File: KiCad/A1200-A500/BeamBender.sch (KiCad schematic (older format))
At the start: 25 parts, among them J1 4-1734742-0, J2 HDMI_A_1.4, J3 STX-3501-3N, U1 LM1117-3.3, U3 ADV7513BSWZ

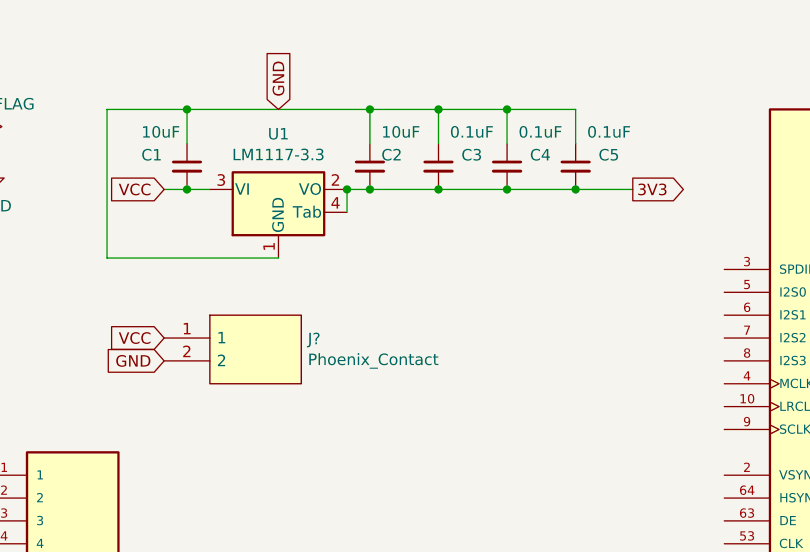
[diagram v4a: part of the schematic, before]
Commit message: Added Polarized electrolytical capacitors for 3V3-power
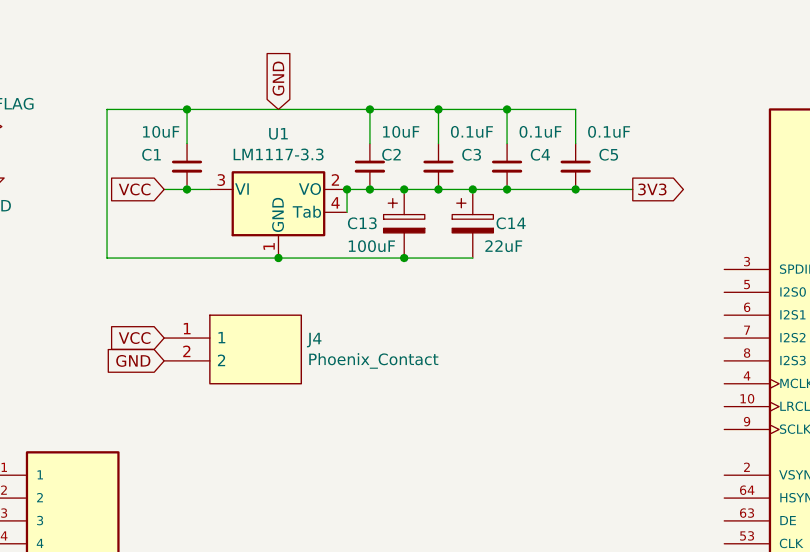
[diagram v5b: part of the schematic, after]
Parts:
- added C13: 100uF, Capacitor_SMD:CP_Elec_6.3x7.7, symbol Device:CP
- added C14: 22uF, Capacitor_SMD:CP_Elec_5x5.8, symbol Device:CP
- gave numbers to parts that had none: 1
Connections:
- net 3V3: now also C13.1, C14.1
- net GND: now also C13.2, C14.2
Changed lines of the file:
@@
 $EndComp
 Wire Wire Line
-	3150 1150 3450 1150
+	3150 1150 3300 1150
 Connection ~ 3450 1150
 Wire Wire Line
@@
 $EndComp
 Wire Wire Line
-	2850 1150 3150 1150
+	2850 1150 3000 1150
 Connection ~ 3150 800
 Wire Wire Line
@@
 	10300 1100 10650 1100
 $Comp
-L BeamBender:Phoenix_Contact J?
+L BeamBender:Phoenix_Contact J4
 U 1 1 654E9506
 P 2350 1850
-F 0 "J?" H 2578 1896 50  0000 L CNN
+F 0 "J4" H 2578 1896 50  0000 L CNN
 F 1 "Phoenix_Contact" H 2578 1805 50  0000 L CNN
 F 2 "BeamBender:Phoenix_Contact" H 2600 2000 50  0001 L CNN
@@
 Text GLabel 1950 1900 0    50   Input ~ 0
 GND
+$Comp
+L Device:CP C13
+U 1 1 65230529
+P 3000 1300
+F 0 "C13" H 2750 1300 50  0000 L CNN
+F 1 "100uF" H 2750 1200 50  0000 L CNN
+F 2 "Capacitor_SMD:CP_Elec_6.3x7.7" H 3038 1150 50  0001 C CNN
+F 3 "~" H 3000 1300 50  0001 C CNN
+	1    3000 1300
+	1    0    0    -1
+$EndComp
+Connection ~ 3000 1150
+Wire Wire Line
+	3000 1150 3150 1150
+Wire Wire Line
+	2450 1450 3000 1450
+Connection ~ 2450 1450
+$Comp
+L Device:CP C14
+U 1 1 65238B23
+P 3300 1300
+F 0 "C14" H 3400 1300 50  0000 L CNN
+F 1 "22uF" H 3350 1200 50  0000 L CNN
+F 2 "Capacitor_SMD:CP_Elec_5x5.8" H 3338 1150 50  0001 C CNN
+F 3 "~" H 3300 1300 50  0001 C CNN
+	1    3300 1300
+	1    0    0    -1
+$EndComp
+Connection ~ 3300 1150
+Wire Wire Line
+	3300 1150 3450 1150
+Wire Wire Line
+	3000 1450 3300 1450
+Connection ~ 3000 1450
 $EndSCHEMATC

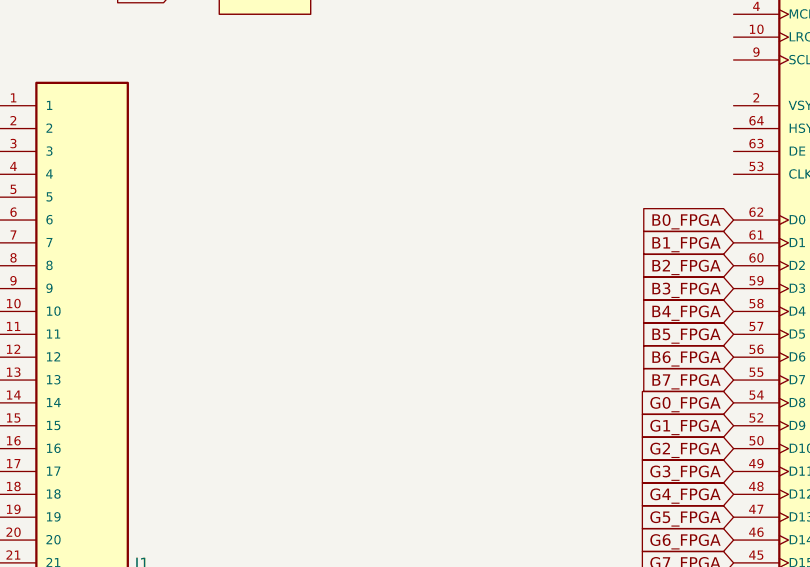
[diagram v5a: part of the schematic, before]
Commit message: Added Gowin FPGA GW1NR-UV9LQ144P
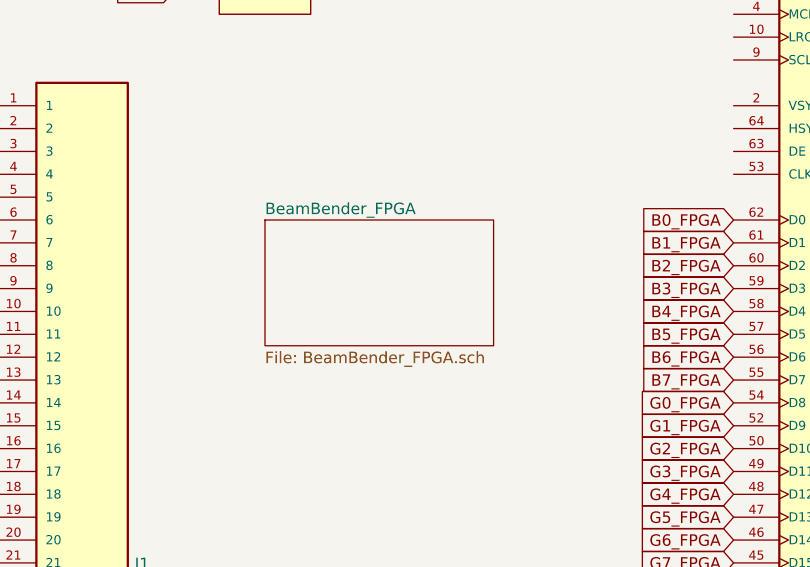
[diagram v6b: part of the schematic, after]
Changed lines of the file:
@@
 $Descr A4 11693 8268
 encoding utf-8
-Sheet 1 1
+Sheet 1 2
 Title ""
 Date ""
@@
 	3000 1450 3300 1450
 Connection ~ 3000 1450
+$Sheet
+S 2350 2900 1000 550
+U 6541C824
+F0 "BeamBender_FPGA" 50
+F1 "BeamBender_FPGA.sch" 50
+$EndSheet
 $EndSCHEMATC

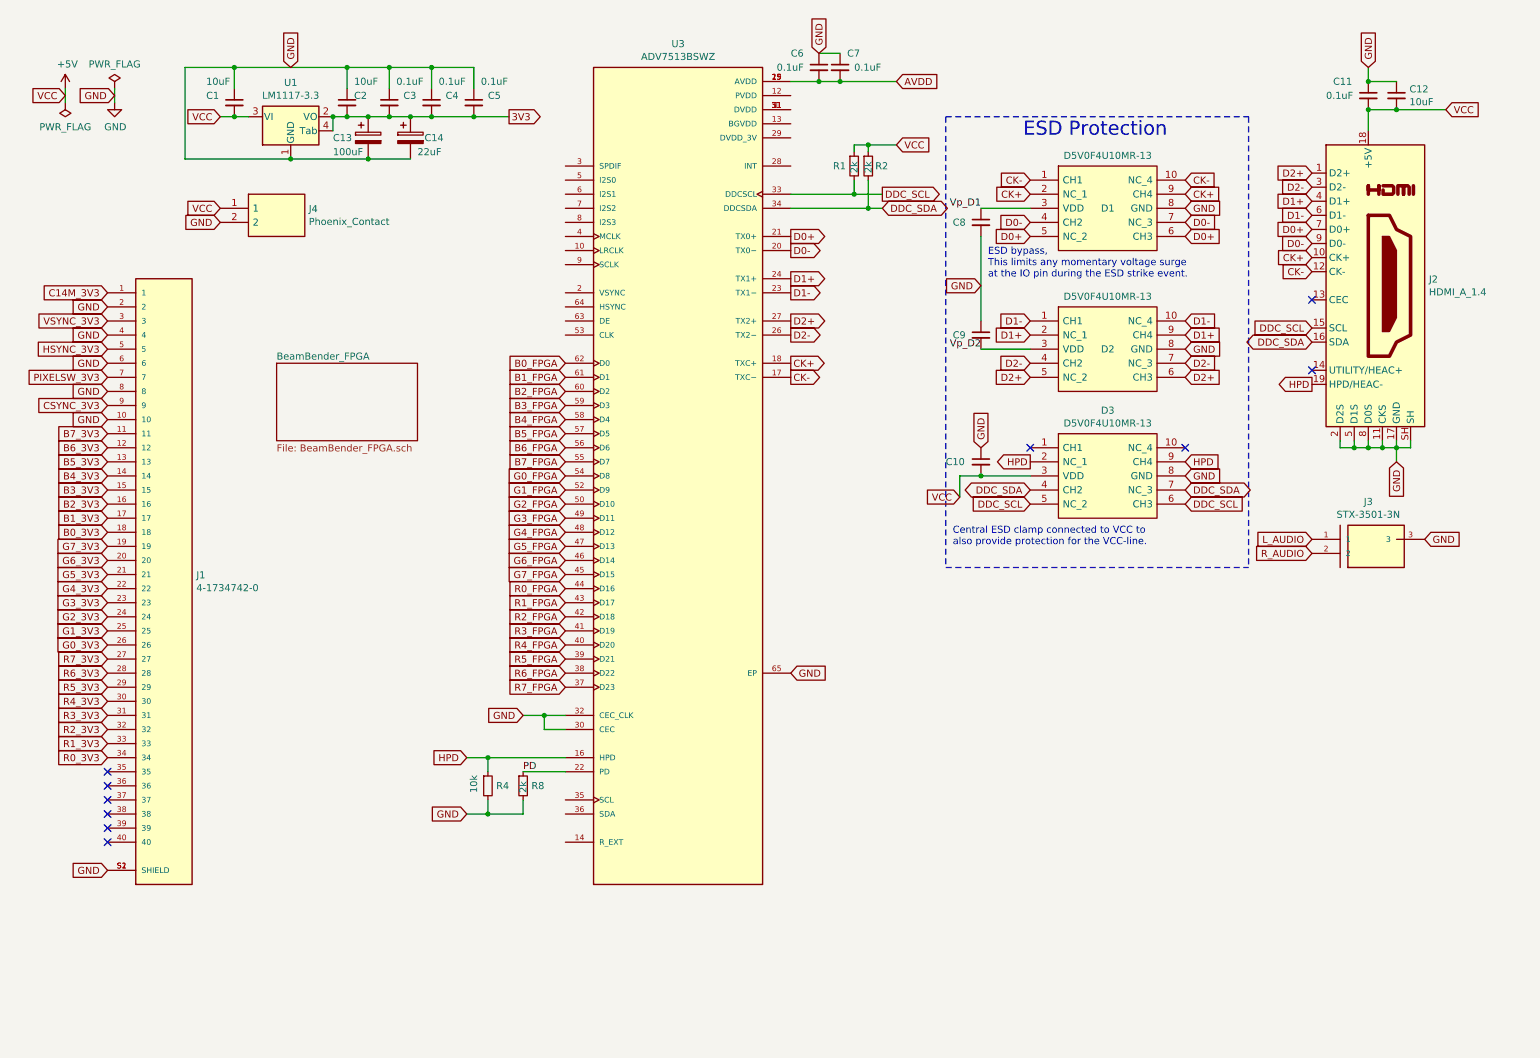
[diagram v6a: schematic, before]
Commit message: Added 27 MHz crystal oscillator X1 to GCLKT_4 pin and did some routing
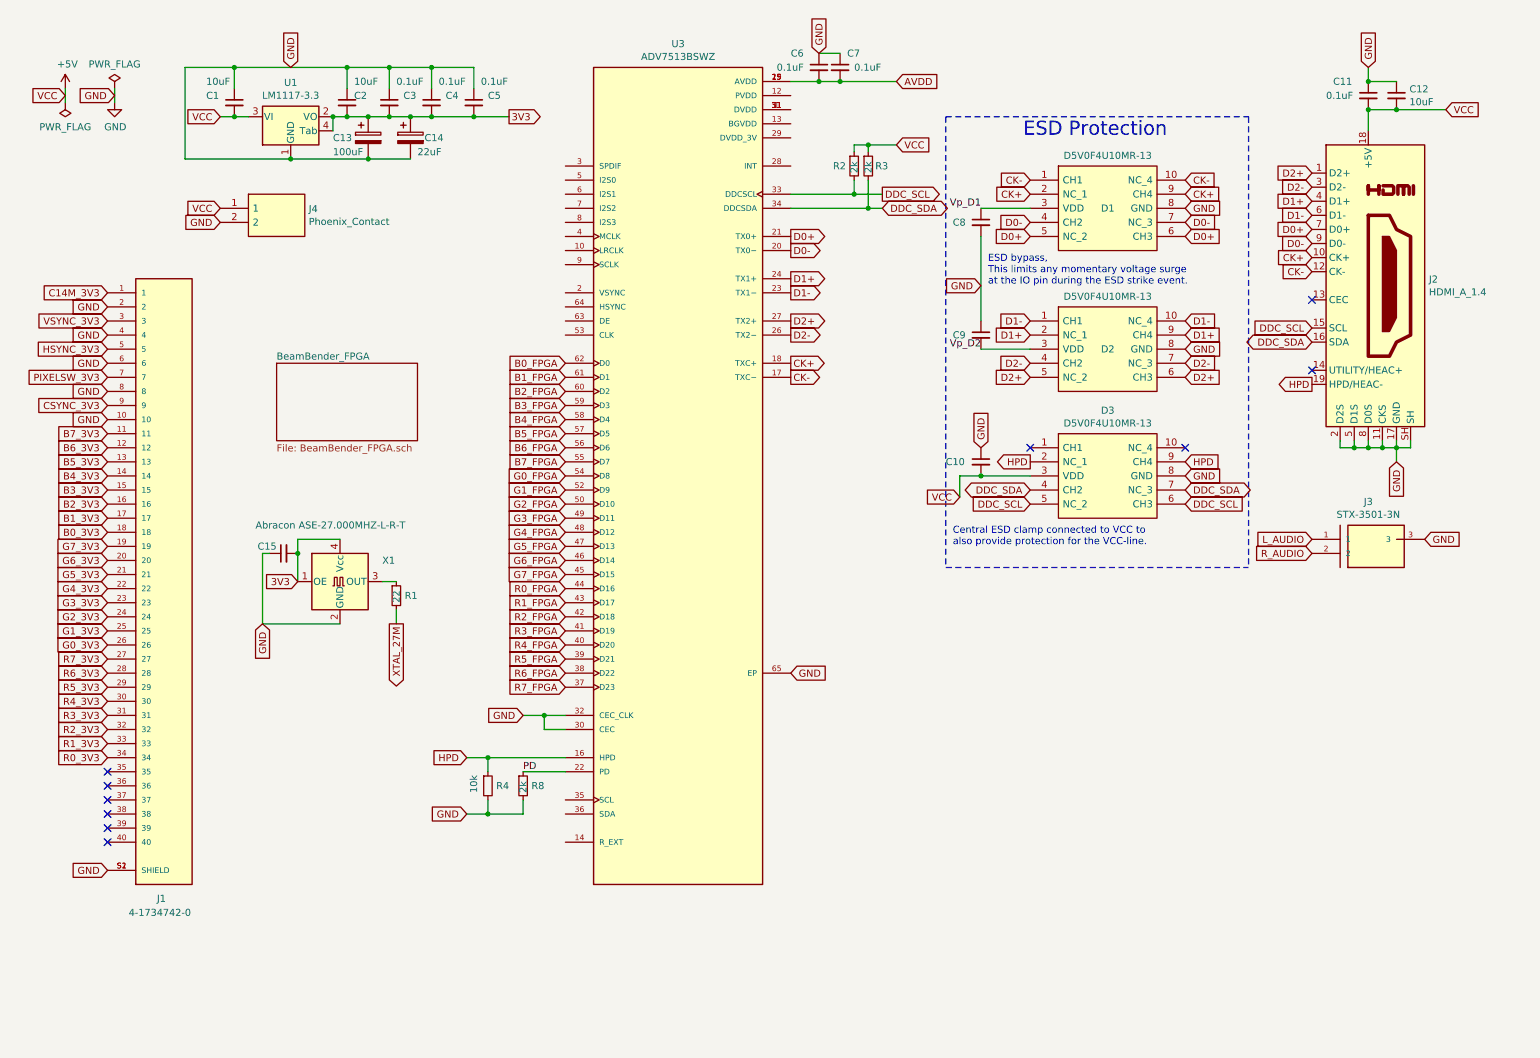
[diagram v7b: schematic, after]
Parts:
- added C15: 0.01uF, Capacitor_SMD:C_0603_1608Metric_Pad1.08x0.95mm_HandSolder, symbol Device:C_Small
- added R1: 22, Resistor_SMD:R_0603_1608Metric_Pad0.98x0.95mm_HandSolder, symbol Device:R_Small
- added X1: Abracon ASE-27.000MHZ-L-R-T, Oscillator:Oscillator_SMD_SeikoEpson_SG8002CE-4Pin_3.2x2.5mm, symbol Oscillator:SG-8002CE
- renumbered R1 to R2, R2 to R3
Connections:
- net 3V3: now also C15.2, X1.1 (OE), X1.4 (Vcc)
- net GND: now also C15.1, X1.2 (GND)
- new net: R1.1, X1.3 (OUT)
- new net XTAL_27M: R1.2
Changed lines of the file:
@@
 U 1 1 64F8C681
 P 1550 4400
-F 0 "J1" H 1780 4396 50  0000 L CNN
-F 1 "4-1734742-0" H 1780 4305 50  0000 L CNN
+F 0 "J1" H 1500 2100 50  0000 L CNN
+F 1 "4-1734742-0" H 1300 2000 50  0000 L CNN
 F 2 "BeamBender:TE_4-1734742-0" H 1550 4400 50  0001 L BNN
 F 3 "" H 1550 4400 50  0001 L BNN
@@
 GND
 $Comp
-L Device:R_Small R2
+L Device:R_Small R3
 U 1 1 6532BC2D
 P 6550 1500
-F 0 "R2" H 6600 1500 50  0000 L CNN
+F 0 "R3" H 6600 1500 50  0000 L CNN
 F 1 "2k" V 6550 1450 50  0000 L CNN
 F 2 "Resistor_SMD:R_0603_1608Metric_Pad0.98x0.95mm_HandSolder" H 6550 1500 50  0001 C CNN
@@
 $EndComp
 $Comp
-L Device:R_Small R1
+L Device:R_Small R2
 U 1 1 6532D8B1
 P 6450 1500
-F 0 "R1" H 6300 1500 50  0000 L CNN
+F 0 "R2" H 6300 1500 50  0000 L CNN
 F 1 "2k" V 6450 1450 50  0000 L CNN
 F 2 "Resistor_SMD:R_0603_1608Metric_Pad0.98x0.95mm_HandSolder" H 6450 1500 50  0001 C CNN
@@
 Text GLabel 7350 3500 1    50   Input ~ 0
 GND
-Text Notes 7400 2300 0    50   ~ 0
+Text Notes 7400 2350 0    50   ~ 0
 ESD bypass, \nThis limits any momentary voltage surge \nat the IO pin during the ESD strike event.
 Text Notes 7150 4200 0    50   ~ 0
@@
 F1 "BeamBender_FPGA.sch" 50
 $EndSheet
+$Comp
+L Oscillator:SG-8002CE X1
+U 1 1 654B3E8F
+P 2800 4450
+F 0 "X1" H 3100 4600 50  0000 L CNN
+F 1 "Abracon ASE-27.000MHZ-L-R-T" H 2200 4850 50  0000 L CNN
+F 2 "Oscillator:Oscillator_SMD_SeikoEpson_SG8002CE-4Pin_3.2x2.5mm" H 3500 4100 50  0001 C CNN
+F 3 "https://www.mouser.com/datasheet/2/3/ASEseries-1774818.pdf" H 2700 4450 50  0001 C CNN
+	1    2800 4450
+	1    0    0    -1
+$EndComp
+Text GLabel 2250 4750 3    50   Input ~ 0
+GND
+Text GLabel 2500 4450 0    50   Input ~ 0
+3V3
+Wire Wire Line
+	2500 4450 2500 4250
+Wire Wire Line
+	2500 4150 2800 4150
+$Comp
+L Device:C_Small C15
+U 1 1 654BAF9D
+P 2400 4250
+F 0 "C15" V 2450 4300 50  0000 L CNN
+F 1 "0.01uF" H 2492 4205 50  0001 L CNN
+F 2 "Capacitor_SMD:C_0603_1608Metric_Pad1.08x0.95mm_HandSolder" H 2400 4250 50  0001 C CNN
+F 3 "~" H 2400 4250 50  0001 C CNN
+	1    2400 4250
+	0    -1   -1   0
+$EndComp
+Connection ~ 2500 4250
+Wire Wire Line
+	2500 4250 2500 4150
+Wire Wire Line
+	2800 4750 2250 4750
+Wire Wire Line
+	2250 4750 2250 4250
+Wire Wire Line
+	2250 4250 2300 4250
+Text GLabel 3200 4750 3    50   Output ~ 0
+XTAL_27M
+$Comp
+L Device:R_Small R1
+U 1 1 65512C64
+P 3200 4550
+F 0 "R1" H 3259 4550 50  0000 L CNN
+F 1 "22" V 3200 4500 50  0000 L CNN
+F 2 "Resistor_SMD:R_0603_1608Metric_Pad0.98x0.95mm_HandSolder" H 3200 4550 50  0001 C CNN
+F 3 "~" H 3200 4550 50  0001 C CNN
+	1    3200 4550
+	1    0    0    -1
+$EndComp
+Wire Wire Line
+	3100 4450 3200 4450
+Wire Wire Line
+	3200 4650 3200 4750
 $EndSCHEMATC
